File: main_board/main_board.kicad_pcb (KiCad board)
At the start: 4 copper layers, 85 x 55 mm, 52 parts, among them J1 USB_B_Micro, J2 Conn_ARM_JTAG_SWD_10, Q1 NX3008PBK,215, Q2 T2N7002AK,LM, U1 SSD1306, U2 ESP32-S2-SOLO, U3 TLV62568PDRLT, U4 MCP73832, Y1 SC32S-7PF20PPM

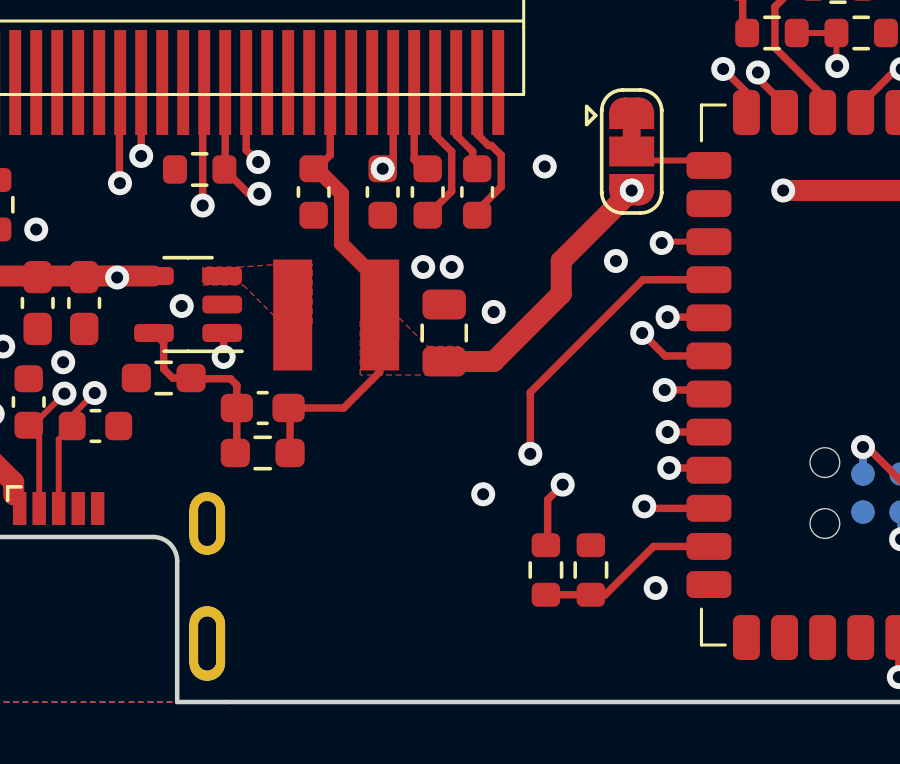
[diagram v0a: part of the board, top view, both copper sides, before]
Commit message: Add more output capacitance to DC/DC
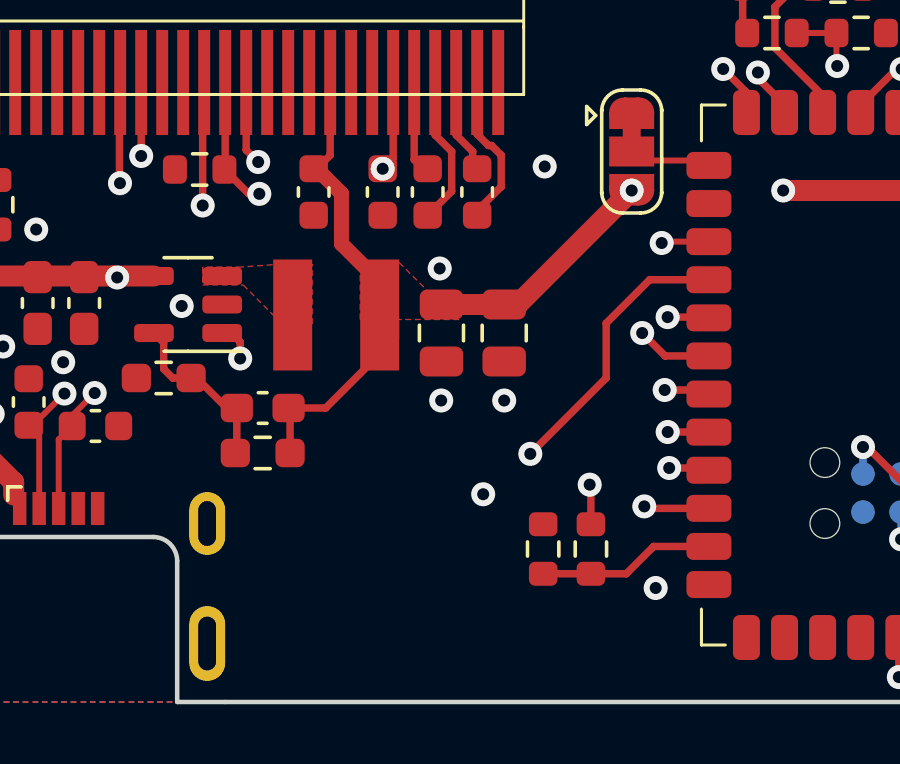
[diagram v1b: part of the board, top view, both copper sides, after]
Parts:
- added C20: 22uF, Capacitor_SMD:C_0805_2012Metric, F.Cu at (130.8, 87.7)
- moved C18 2.00 mm to (132.8, 87.7), turned to -90 degrees
- moved R10 1.74 mm to (134.2, 94.9)
- moved R5 1.66 mm to (135.7, 94.9)
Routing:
- net +3V3: track 77.3 -> 75.7 mm
- net +BATT: track 80.6 -> 81.7 mm
- net +5V: track 28.6 -> 28.0 mm
- net GND: vias 28 -> 27

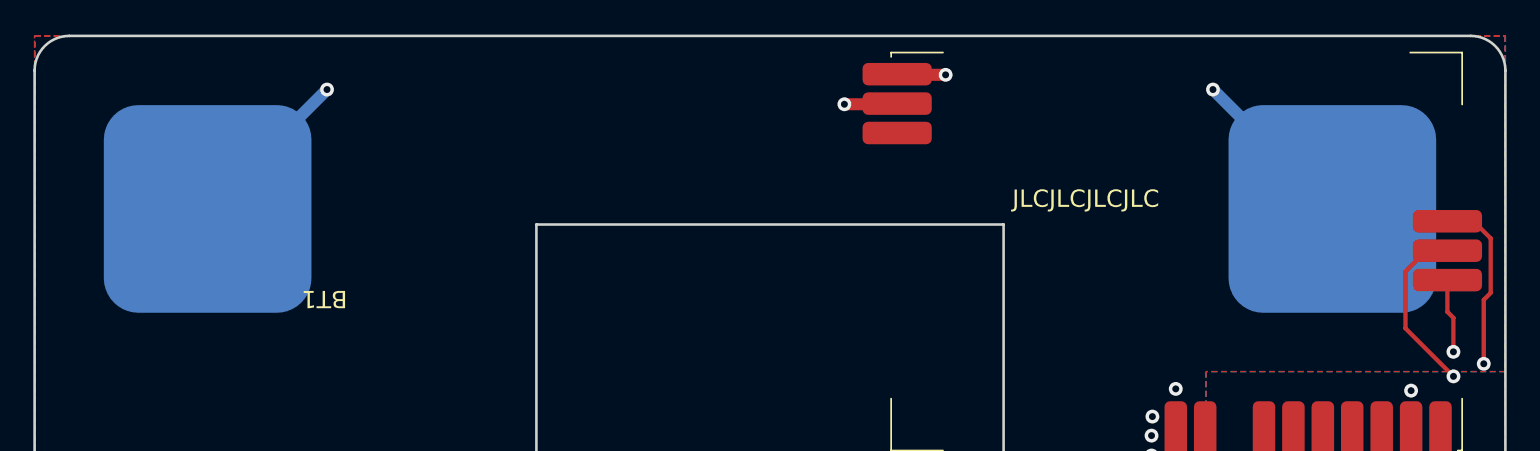
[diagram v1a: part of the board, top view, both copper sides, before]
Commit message: Move electrodes a bit
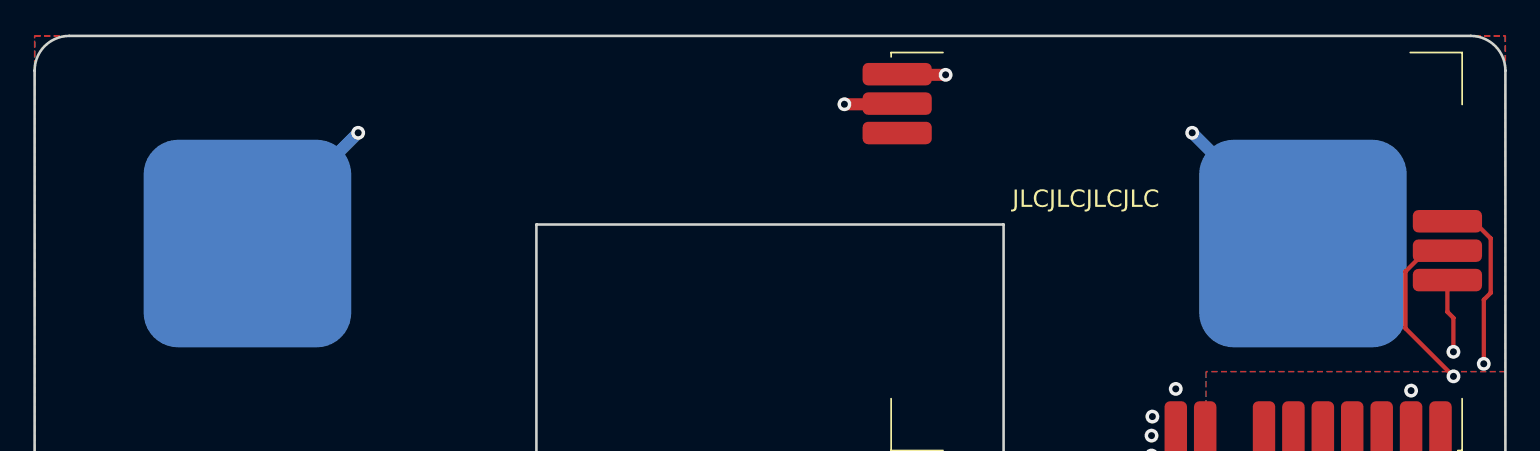
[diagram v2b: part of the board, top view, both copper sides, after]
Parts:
- moved ER1 3.05 mm to (92.3, 57.0)
- moved EL1 2.62 mm to (153.3, 57.0)
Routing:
- net Net-(M1-ECG_R): track 43.1 -> 38.6 mm
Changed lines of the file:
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@@
     (property "ki_keywords" "battery cell")
     (attr smd)
-    (fp_text reference "BT1" (at 0.05 -13 180 unlocked) (layer "F.SilkS")
+    (fp_text reference "BT1" (at 0.05 -13 180 unlocked) (layer "F.SilkS") hide
         (effects (font (size 1 1) (thickness 0.1)))
     )
@@
   )
   (footprint "main_board_parts:Electrode" locked (layer "B.Cu")
-    (at 90 55 180)
+    (at 92.3 57 180)
     (property "Sheetfile" "main_board.kicad_sch")
     (property "Sheetname" "")
@@
     )
     (fp_text value "~" (at 0 -9.5 unlocked) (layer "B.Fab") hide
-        (effects (font (size 1 1) (thickness 0.15)) (justify mirror))
-    )
-    (fp_text user "${REFERENCE}" (at 0 -11 unlocked) (layer "B.Fab")
         (effects (font (size 1 1) (thickness 0.15)) (justify mirror))
     )
@@
   )
   (footprint "main_board_parts:Electrode" locked (layer "B.Cu")
-    (at 155 55 180)
+    (at 153.3 57 180)
     (property "Sheetfile" "main_board.kicad_sch")
     (property "Sheetname" "")
@@
     )
     (fp_text value "~" (at 0 -9.5 unlocked) (layer "B.Fab") hide
-        (effects (font (size 1 1) (thickness 0.15)) (justify mirror))
-    )
-    (fp_text user "${REFERENCE}" (at 0 -11 unlocked) (layer "B.Fab")
         (effects (font (size 1 1) (thickness 0.15)) (justify mirror))
     )
@@
   (gr_line (start 110 86.3) (end 80 86.3)
     (stroke (width 0.15) (type default)) (layer "Dwgs.User"))
-  (gr_arc (start 80 47) (mid 80.585786 45.585786) (end 82 45)
+  (gr_arc locked (start 80 47) (mid 80.585786 45.585786) (end 82 45)
     (stroke (width 0.15) (type default)) (layer "Edge.Cuts"))
-  (gr_arc (start 165 98) (mid 164.414214 99.414214) (end 163 100)
+  (gr_arc locked (start 165 98) (mid 164.414214 99.414214) (end 163 100)
     (stroke (width 0.15) (type default)) (layer "Edge.Cuts"))
   (gr_line locked (start 129.5 75.4) (end 136 75.4)
     (stroke (width 0.15) (type default)) (layer "Edge.Cuts"))
-  (gr_line (start 123.55 100) (end 163 100)
+  (gr_line locked (start 123.55 100) (end 163 100)
     (stroke (width 0.15) (type default)) (layer "Edge.Cuts"))
-  (gr_line (start 82 45) (end 163 45)
+  (gr_line locked (start 82 45) (end 163 45)
     (stroke (width 0.15) (type default)) (layer "Edge.Cuts"))
-  (gr_line (start 82 100) (end 111.95 100)
+  (gr_line locked (start 82 100) (end 111.95 100)
     (stroke (width 0.15) (type default)) (layer "Edge.Cuts"))
-  (gr_line (start 80 98) (end 80 47)
+  (gr_line locked (start 80 98) (end 80 47)
     (stroke (width 0.15) (type default)) (layer "Edge.Cuts"))
   (gr_line locked (start 136 55.9) (end 136 75.4)
     (stroke (width 0.15) (type default)) (layer "Edge.Cuts"))
-  (gr_arc (start 163 45) (mid 164.414214 45.585786) (end 165 47)
+  (gr_arc locked (start 163 45) (mid 164.414214 45.585786) (end 165 47)
     (stroke (width 0.15) (type default)) (layer "Edge.Cuts"))
   (gr_line locked (start 115.5 75.4) (end 115.5 76.4)
@@
   (gr_line locked (start 129.5 76.4) (end 129.5 75.4)
     (stroke (width 0.15) (type default)) (layer "Edge.Cuts"))
-  (gr_arc (start 82 100) (mid 80.585786 99.414214) (end 80 98)
+  (gr_arc locked (start 82 100) (mid 80.585786 99.414214) (end 80 98)
     (stroke (width 0.15) (type default)) (layer "Edge.Cuts"))
-  (gr_line (start 165 47) (end 165 98)
+  (gr_line locked (start 165 47) (end 165 98)
     (stroke (width 0.15) (type default)) (layer "Edge.Cuts"))
   (gr_line locked (start 115.5 76.4) (end 129.5 76.4)
@@
   (segment (start 129.8875 47.25) (end 129.85 47.2125) (width 0.7) (layer "F.Cu") (net 1))
   (segment (start 132.65 47.25) (end 129.8875 47.25) (width 0.7) (layer "F.Cu") (net 1))
-  (via (at 148.1 48.1) (size 0.8) (drill 0.4) (layers "F.Cu" "B.Cu") (net 1))
+  (via (at 146.9 50.6) (size 0.8) (drill 0.4) (layers "F.Cu" "B.Cu") (net 1))
   (via (at 132.65 47.25) (size 0.8) (drill 0.4) (layers "F.Cu" "B.Cu") (net 1))
-  (segment (start 148.1 48.1) (end 133.5 48.1) (width 0.7) (layer "In1.Cu") (net 1))
-  (segment (start 133.5 48.1) (end 132.65 47.25) (width 0.7) (layer "In1.Cu") (net 1))
-  (segment (start 155 55) (end 148.1 48.1) (width 0.7) (layer "B.Cu") (net 1))
+  (segment (start 136 50.6) (end 132.65 47.25) (width 0.7) (layer "In1.Cu") (net 1))
+  (segment (start 146.9 50.6) (end 136 50.6) (width 0.7) (layer "In1.Cu") (net 1))
+  (segment (start 146.9 50.6) (end 151.3 55) (width 0.7) (layer "B.Cu") (net 1))
+  (segment (start 151.3 55) (end 155 55) (width 0.7) (layer "B.Cu") (net 1))
   (segment (start 126.875 48.95) (end 126.8375 48.9125) (width 0.7) (layer "F.Cu") (net 2))
   (segment (start 126.8375 48.9125) (end 126.8 48.95) (width 0.5) (layer "F.Cu") (net 2))
@@
   (segment (start 129.8125 48.95) (end 126.875 48.95) (width 0.7) (layer "F.Cu") (net 2))
   (via (at 126.8 48.95) (size 0.8) (drill 0.4) (layers "F.Cu" "B.Cu") (net 2))
-  (via (at 96.9 48.1) (size 0.8) (drill 0.4) (layers "F.Cu" "B.Cu") (net 2))
-  (segment (start 96.9 48.1) (end 125.95 48.1) (width 0.7) (layer "In1.Cu") (net 2))
-  (segment (start 125.95 48.1) (end 126.8 48.95) (width 0.7) (layer "In1.Cu") (net 2))
-  (segment (start 90 55) (end 96.9 48.1) (width 0.7) (layer "B.Cu") (net 2))
+  (via (at 98.7 50.6) (size 0.8) (drill 0.4) (layers "F.Cu" "B.Cu") (net 2))
+  (segment (start 98.7 50.6) (end 100.35 48.95) (width 0.7) (layer "In1.Cu") (net 2))
+  (segment (start 100.35 48.95) (end 126.8 48.95) (width 0.7) (layer "In1.Cu") (net 2))
+  (segment (start 93.85 55) (end 94.3 55) (width 0.7) (layer "B.Cu") (net 2))
+  (segment (start 94.3 55) (end 98.7 50.6) (width 0.7) (layer "B.Cu") (net 2))
   (segment (start 104.8 92.2) (end 105.2875 91.7125) (width 0.5) (layer "F.Cu") (net 3))
   (segment (start 139.82 73.9925) (end 139.82 73.9175) (width 0.25) (layer "F.Cu") (net 3))

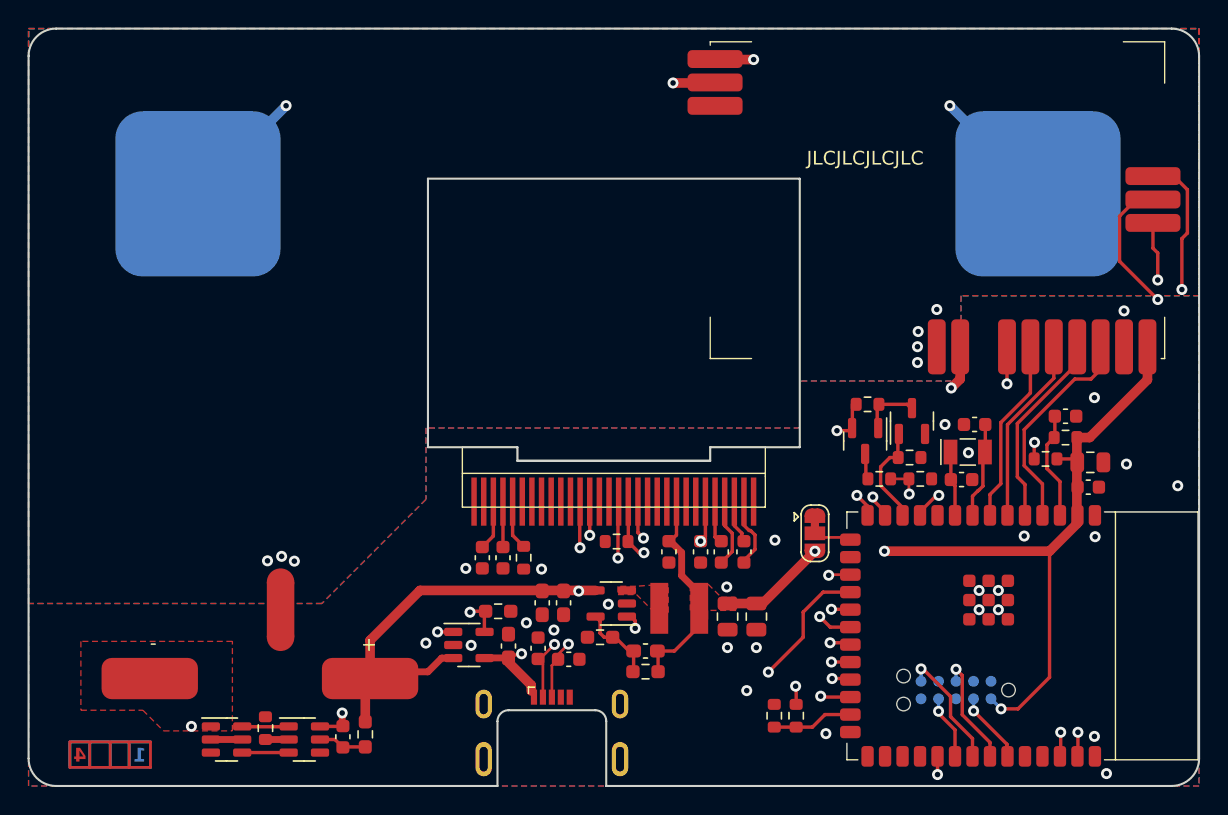
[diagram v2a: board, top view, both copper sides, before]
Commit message: Move frontend away from the edge
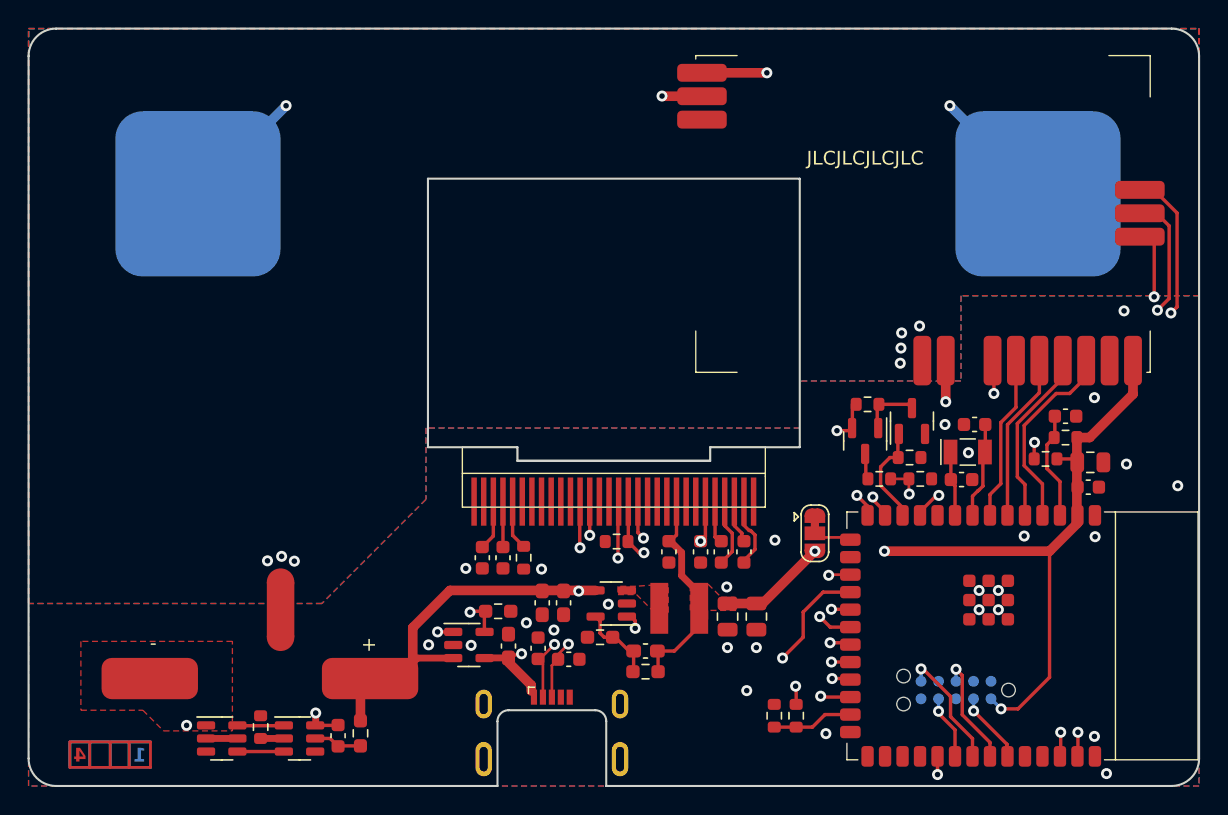
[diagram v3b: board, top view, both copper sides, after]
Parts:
- moved M1 1.45 mm to (128.7, 69.7)
- moved C14 0.36 mm to (102.5, 96.3)
- moved R15 0.36 mm to (96.8, 95.7)
- moved R6 0.36 mm to (104.1, 96.2)
- moved U5 0.36 mm to (99.7, 96.5)
- moved U6 0.36 mm to (94.0, 96.5)
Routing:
- net /ECG_EN: track 46.2 -> 44.3 mm
- net Net-(BT1--): track 14.0 -> 12.3 mm
- net Net-(M1-~{DRDY}): track 15.8 -> 14.2 mm
- net /~{TOUCH}: track 47.4 -> 45.8 mm
- net Net-(M1-MISO): track 14.3 -> 12.8 mm
- net Net-(M1-MOSI): track 13.5 -> 12.0 mm
- net +3V3: track 75.7 -> 74.2 mm
- net Net-(M1-SCLK): track 13.6 -> 12.2 mm
- net Net-(M1-ECG_R): track 38.6 -> 37.2 mm
- net Net-(M1-~{CS}): track 19.6 -> 18.4 mm
- net /CHG_CURRENT: track 35.7 -> 35.1 mm
- net Net-(M1-ECG_L): track 28.4 -> 28.9 mm
- net +BATT: track 81.7 -> 81.1 mm

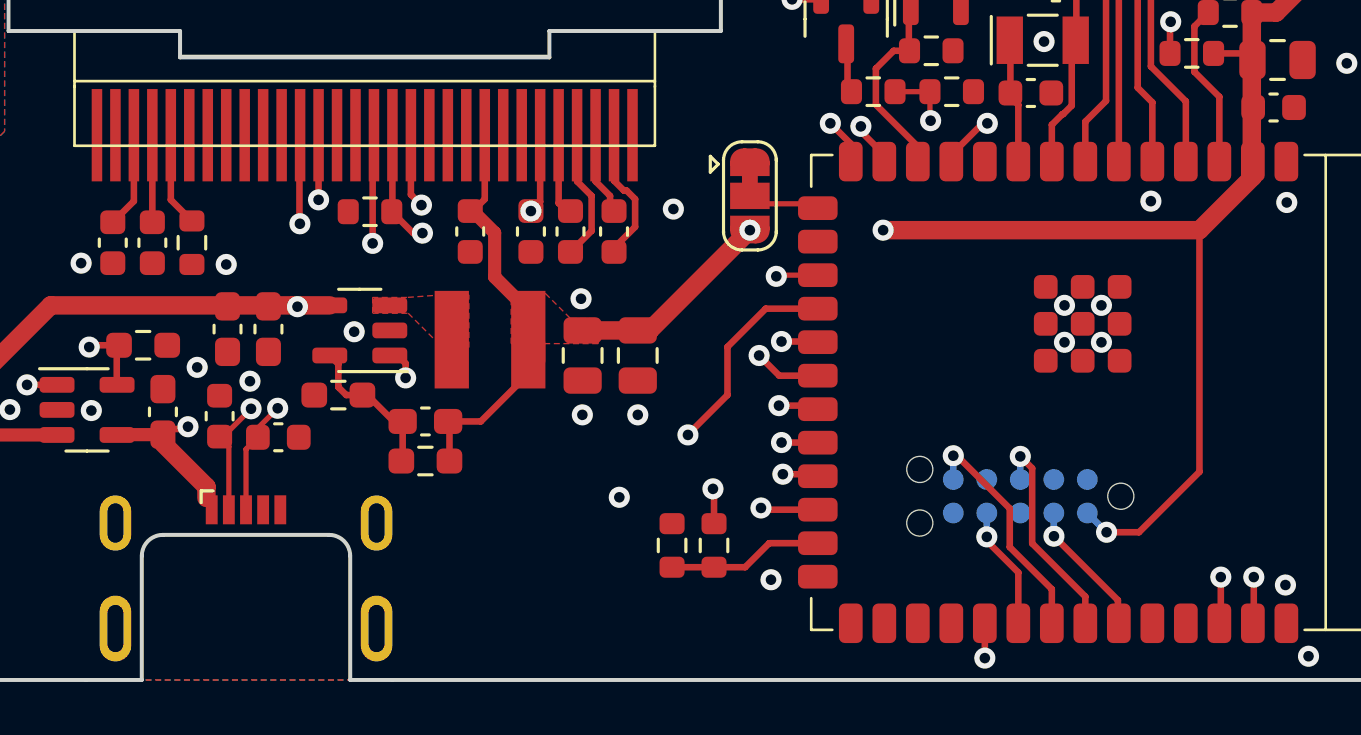
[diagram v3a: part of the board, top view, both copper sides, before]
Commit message: Fix #24: move VBUS detect to IO17
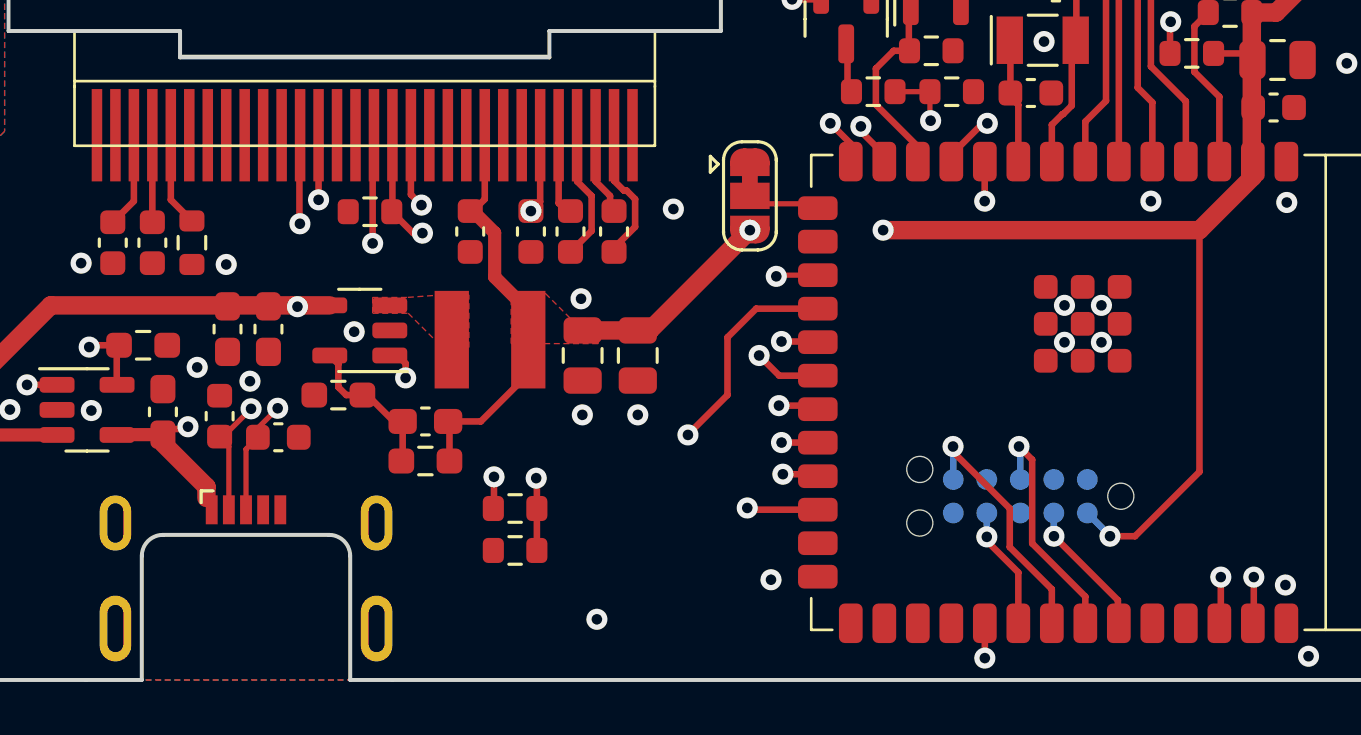
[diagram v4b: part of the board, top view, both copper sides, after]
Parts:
- moved R5 7.67 mm to (128.2, 93.5), turned to 0 degrees
- moved R10 5.95 mm to (128.2, 95.1), turned to 180 degrees
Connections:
- U2 pad 10: unconnected-(U2-IO17-Pad10) -> /VBUS_DETECT
- U2 pad 25: /VBUS_DETECT -> unconnected-(U2-IO34-Pad25)
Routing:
- net /VBUS_DETECT: track 5.90 -> 28.7 mm, vias 0 -> 2
- net +5V: track 28.0 -> 19.2 mm
- net Net-(J2-NC/TDI): track 8.22 -> 9.01 mm
- net Net-(J2-SWO/TDO): track 8.88 -> 9.51 mm
- net +3V3: track 74.2 -> 73.7 mm
